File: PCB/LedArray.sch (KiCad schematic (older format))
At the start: 20 parts, among them Q2 2N3904, Q3 2N3904, Q4 2N3904, Q5 2N3904, Q6 2N3904

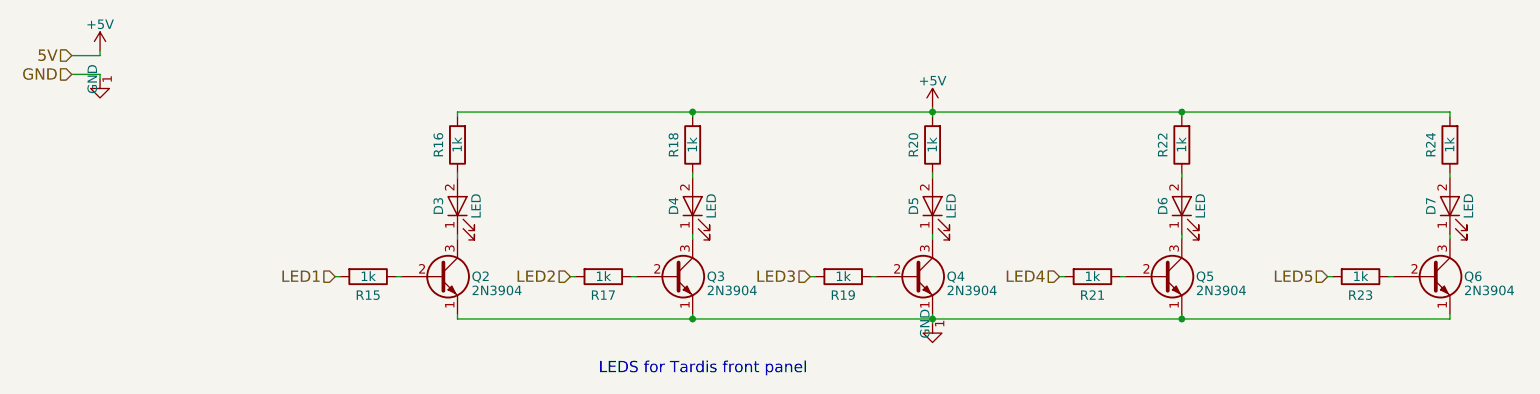
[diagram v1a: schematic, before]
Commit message: Added PCB layout
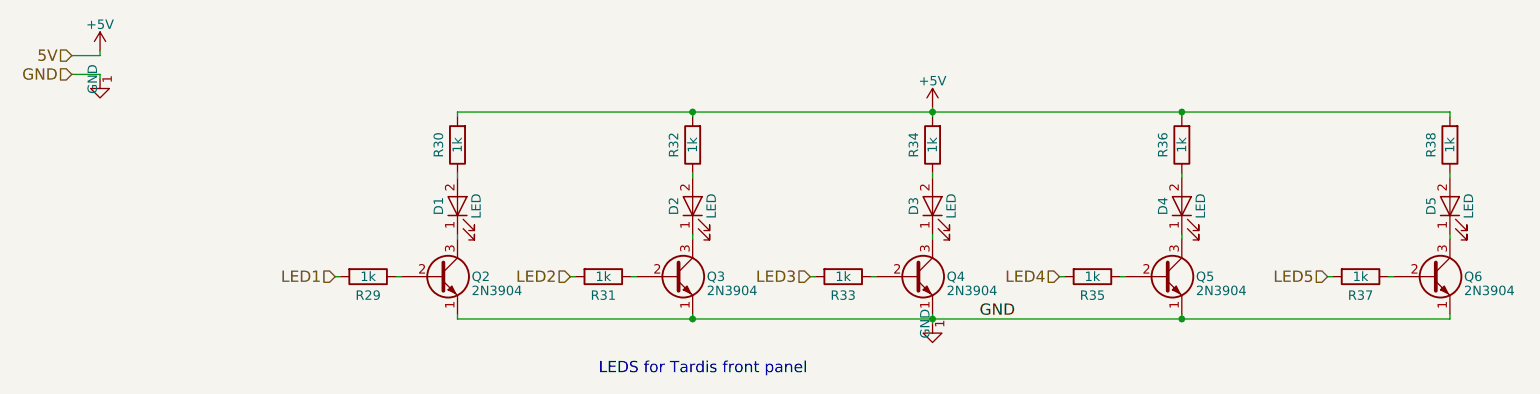
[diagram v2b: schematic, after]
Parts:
- D1: renamed from D3; footprint (none) -> LEDs:LED_D5.0mm
- D2: renamed from D4; footprint (none) -> LEDs:LED_D5.0mm
- D3: renamed from D5; footprint (none) -> LEDs:LED_D5.0mm
- D4: renamed from D6; footprint (none) -> LEDs:LED_D5.0mm
- D5: renamed from D7; footprint (none) -> LEDs:LED_D5.0mm
- Q2, Q3, Q4, Q5, Q6: footprint (none) -> TO_SOT_Packages_THT:TO-92_Molded_Narrow
- R29: renamed from R15; footprint (none) -> Resistors_SMD:R_0603_HandSoldering
- R30: renamed from R16; footprint (none) -> Resistors_SMD:R_0603_HandSoldering
- R31: renamed from R17; footprint (none) -> Resistors_SMD:R_0603_HandSoldering
- R32: renamed from R18; footprint (none) -> Resistors_SMD:R_0603_HandSoldering
- R33: renamed from R19; footprint (none) -> Resistors_SMD:R_0603_HandSoldering
- R34: renamed from R20; footprint (none) -> Resistors_SMD:R_0603_HandSoldering
- R35: renamed from R21; footprint (none) -> Resistors_SMD:R_0603_HandSoldering
- R36: renamed from R22; footprint (none) -> Resistors_SMD:R_0603_HandSoldering
- R37: renamed from R23; footprint (none) -> Resistors_SMD:R_0603_HandSoldering
- R38: renamed from R24; footprint (none) -> Resistors_SMD:R_0603_HandSoldering
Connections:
- net GND: now also Q2.1 (E), Q3.1 (E), Q4.1 (E), Q5.1 (E), Q6.1 (E)
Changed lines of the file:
@@
 $EndDescr
 $Comp
-L LED D7
+L LED D5
 U 1 1 5A1C9FD6
 P 8750 3800
-F 0 "D7" H 8750 3900 50  0000 C CNN
+F 0 "D5" H 8750 3900 50  0000 C CNN
 F 1 "LED" H 8750 3700 50  0000 C CNN
-F 2 "" H 8750 3800 50  0001 C CNN
+F 2 "LEDs:LED_D5.0mm" H 8750 3800 50  0001 C CNN
 F 3 "" H 8750 3800 50  0001 C CNN
 	1    8750 3800
@@
 $EndComp
 $Comp
-L R R24
+L R R38
 U 1 1 5A1C9FDD
 P 8750 3475
-F 0 "R24" V 8850 3475 50  0000 C CNN
+F 0 "R38" V 8850 3475 50  0000 C CNN
 F 1 "1k" V 8750 3475 50  0000 C CNN
-F 2 "" V 8680 3475 50  0001 C CNN
+F 2 "Resistors_SMD:R_0603_HandSoldering" V 8680 3475 50  0001 C CNN
 F 3 "" H 8750 3475 50  0001 C CNN
 	1    8750 3475
@@
 $EndComp
 $Comp
-L R R23
+L R R37
 U 1 1 5A1C9FE4
 P 8275 4175
-F 0 "R23" V 8375 4175 50  0000 C CNN
+F 0 "R37" V 8375 4175 50  0000 C CNN
 F 1 "1k" V 8275 4175 50  0000 C CNN
-F 2 "" V 8205 4175 50  0001 C CNN
+F 2 "Resistors_SMD:R_0603_HandSoldering" V 8205 4175 50  0001 C CNN
 F 3 "" H 8275 4175 50  0001 C CNN
 	1    8275 4175
@@
 	8750 3625 8750 3650
 $Comp
-L LED D6
+L LED D4
 U 1 1 5A1CA001
 P 7325 3800
-F 0 "D6" H 7325 3900 50  0000 C CNN
+F 0 "D4" H 7325 3900 50  0000 C CNN
 F 1 "LED" H 7325 3700 50  0000 C CNN
-F 2 "" H 7325 3800 50  0001 C CNN
+F 2 "LEDs:LED_D5.0mm" H 7325 3800 50  0001 C CNN
 F 3 "" H 7325 3800 50  0001 C CNN
 	1    7325 3800
@@
 $EndComp
 $Comp
-L R R22
+L R R36
 U 1 1 5A1CA008
 P 7325 3475
-F 0 "R22" V 7425 3475 50  0000 C CNN
+F 0 "R36" V 7425 3475 50  0000 C CNN
 F 1 "1k" V 7325 3475 50  0000 C CNN
-F 2 "" V 7255 3475 50  0001 C CNN
+F 2 "Resistors_SMD:R_0603_HandSoldering" V 7255 3475 50  0001 C CNN
 F 3 "" H 7325 3475 50  0001 C CNN
 	1    7325 3475
@@
 $EndComp
 $Comp
-L R R21
+L R R35
 U 1 1 5A1CA00F
 P 6850 4175
-F 0 "R21" V 6950 4175 50  0000 C CNN
+F 0 "R35" V 6950 4175 50  0000 C CNN
 F 1 "1k" V 6850 4175 50  0000 C CNN
-F 2 "" V 6780 4175 50  0001 C CNN
+F 2 "Resistors_SMD:R_0603_HandSoldering" V 6780 4175 50  0001 C CNN
 F 3 "" H 6850 4175 50  0001 C CNN
 	1    6850 4175
@@
 	7325 3625 7325 3650
 $Comp
-L LED D5
+L LED D3
 U 1 1 5A1CA02C
 P 6000 3800
-F 0 "D5" H 6000 3900 50  0000 C CNN
+F 0 "D3" H 6000 3900 50  0000 C CNN
 F 1 "LED" H 6000 3700 50  0000 C CNN
-F 2 "" H 6000 3800 50  0001 C CNN
+F 2 "LEDs:LED_D5.0mm" H 6000 3800 50  0001 C CNN
 F 3 "" H 6000 3800 50  0001 C CNN
 	1    6000 3800
@@
 $EndComp
 $Comp
-L R R20
+L R R34
 U 1 1 5A1CA033
 P 6000 3475
-F 0 "R20" V 6100 3475 50  0000 C CNN
+F 0 "R34" V 6100 3475 50  0000 C CNN
 F 1 "1k" V 6000 3475 50  0000 C CNN
-F 2 "" V 5930 3475 50  0001 C CNN
+F 2 "Resistors_SMD:R_0603_HandSoldering" V 5930 3475 50  0001 C CNN
 F 3 "" H 6000 3475 50  0001 C CNN
 	1    6000 3475
@@
 $EndComp
 $Comp
-L R R19
+L R R33
 U 1 1 5A1CA03A
 P 5525 4175
-F 0 "R19" V 5625 4175 50  0000 C CNN
+F 0 "R33" V 5625 4175 50  0000 C CNN
 F 1 "1k" V 5525 4175 50  0000 C CNN
-F 2 "" V 5455 4175 50  0001 C CNN
+F 2 "Resistors_SMD:R_0603_HandSoldering" V 5455 4175 50  0001 C CNN
 F 3 "" H 5525 4175 50  0001 C CNN
 	1    5525 4175
@@
 	6000 3625 6000 3650
 $Comp
-L LED D4
+L LED D2
 U 1 1 5A1CA057
 P 4725 3800
-F 0 "D4" H 4725 3900 50  0000 C CNN
+F 0 "D2" H 4725 3900 50  0000 C CNN
 F 1 "LED" H 4725 3700 50  0000 C CNN
-F 2 "" H 4725 3800 50  0001 C CNN
+F 2 "LEDs:LED_D5.0mm" H 4725 3800 50  0001 C CNN
 F 3 "" H 4725 3800 50  0001 C CNN
 	1    4725 3800
@@
 $EndComp
 $Comp
-L R R18
+L R R32
 U 1 1 5A1CA05E
 P 4725 3475
-F 0 "R18" V 4825 3475 50  0000 C CNN
+F 0 "R32" V 4825 3475 50  0000 C CNN
 F 1 "1k" V 4725 3475 50  0000 C CNN
-F 2 "" V 4655 3475 50  0001 C CNN
+F 2 "Resistors_SMD:R_0603_HandSoldering" V 4655 3475 50  0001 C CNN
 F 3 "" H 4725 3475 50  0001 C CNN
 	1    4725 3475
@@
 $EndComp
 $Comp
-L R R17
+L R R31
 U 1 1 5A1CA065
 P 4250 4175
-F 0 "R17" V 4350 4175 50  0000 C CNN
+F 0 "R31" V 4350 4175 50  0000 C CNN
 F 1 "1k" V 4250 4175 50  0000 C CNN
-F 2 "" V 4180 4175 50  0001 C CNN
+F 2 "Resistors_SMD:R_0603_HandSoldering" V 4180 4175 50  0001 C CNN
 F 3 "" H 4250 4175 50  0001 C CNN
 	1    4250 4175
@@
 	4725 3625 4725 3650
 $Comp
-L LED D3
+L LED D1
 U 1 1 5A1CA082
 P 3475 3800
-F 0 "D3" H 3475 3900 50  0000 C CNN
+F 0 "D1" H 3475 3900 50  0000 C CNN
 F 1 "LED" H 3475 3700 50  0000 C CNN
-F 2 "" H 3475 3800 50  0001 C CNN
+F 2 "LEDs:LED_D5.0mm" H 3475 3800 50  0001 C CNN
 F 3 "" H 3475 3800 50  0001 C CNN
 	1    3475 3800
@@
 $EndComp
 $Comp
-L R R16
+L R R30
 U 1 1 5A1CA089
 P 3475 3475
-F 0 "R16" V 3575 3475 50  0000 C CNN
+F 0 "R30" V 3575 3475 50  0000 C CNN
 F 1 "1k" V 3475 3475 50  0000 C CNN
-F 2 "" V 3405 3475 50  0001 C CNN
+F 2 "Resistors_SMD:R_0603_HandSoldering" V 3405 3475 50  0001 C CNN
 F 3 "" H 3475 3475 50  0001 C CNN
 	1    3475 3475
@@
 $EndComp
 $Comp
-L R R15
+L R R29
 U 1 1 5A1CA090
 P 3000 4175
-F 0 "R15" V 3100 4175 50  0000 C CNN
+F 0 "R29" V 3100 4175 50  0000 C CNN
 F 1 "1k" V 3000 4175 50  0000 C CNN
-F 2 "" V 2930 4175 50  0001 C CNN
+F 2 "Resistors_SMD:R_0603_HandSoldering" V 2930 4175 50  0001 C CNN
 F 3 "" H 3000 4175 50  0001 C CNN
 	1    3000 4175
@@
 GND
 $Comp
-L GND-RESCUE-Tardis #PWR059
+L GND-RESCUE-Tardis #PWR058
 U 1 1 5A34958F
 P 1575 3125
-AR Path="/5A34958F" Ref="#PWR059"  Part="1"
-AR Path="/5A1C89E5/5A34958F" Ref="#PWR63"  Part="1"
-F 0 "#PWR63" H 1575 2875 50  0001 C CNN
+F 0 "#PWR058" H 1575 2875 50  0001 C CNN
 F 1 "GND" H 1575 2975 50  0001 C CNN
 F 2 "" H 1575 3125 50  0001 C CNN
@@
 	1575 3100 1575 3125
 $Comp
-L +5V #PWR62
+L +5V #PWR059
 U 1 1 5A349597
 P 1575 2975
-F 0 "#PWR62" H 1575 2825 50  0001 C CNN
+F 0 "#PWR059" H 1575 2825 50  0001 C CNN
 F 1 "+5V" H 1575 3115 50  0000 C CNN
 F 2 "" H 1575 2975 50  0001 C CNN
@@
 	1575 3000 1575 2975
 $Comp
-L +5V #PWR64
+L +5V #PWR060
 U 1 1 5A349B68
 P 6000 3275
-F 0 "#PWR64" H 6000 3125 50  0001 C CNN
+F 0 "#PWR060" H 6000 3125 50  0001 C CNN
 F 1 "+5V" H 6000 3415 50  0000 C CNN
 F 2 "" H 6000 3275 50  0001 C CNN
@@
 $EndComp
 $Comp
-L GND-RESCUE-Tardis #PWR062
+L GND-RESCUE-Tardis #PWR061
 U 1 1 5A349BAF
 P 6000 4425
-AR Path="/5A349BAF" Ref="#PWR062"  Part="1"
-AR Path="/5A1C89E5/5A349BAF" Ref="#PWR65"  Part="1"
-F 0 "#PWR65" H 6000 4175 50  0001 C CNN
+F 0 "#PWR061" H 6000 4175 50  0001 C CNN
 F 1 "GND" H 6000 4275 50  0001 C CNN
 F 2 "" H 6000 4425 50  0001 C CNN
@@
 F 0 "Q2" H 3550 4175 50  0000 L CNN
 F 1 "2N3904" H 3550 4100 50  0000 L CNN
-F 2 "" H 3575 4275 50  0001 C CNN
+F 2 "TO_SOT_Packages_THT:TO-92_Molded_Narrow" H 3575 4275 50  0001 C CNN
 F 3 "" H 3375 4175 50  0001 C CNN
 	1    3375 4175
@@
 F 0 "Q3" H 4800 4175 50  0000 L CNN
 F 1 "2N3904" H 4800 4100 50  0000 L CNN
-F 2 "" H 4825 4275 50  0001 C CNN
+F 2 "TO_SOT_Packages_THT:TO-92_Molded_Narrow" H 4825 4275 50  0001 C CNN
 F 3 "" H 4625 4175 50  0001 C CNN
 	1    4625 4175
@@
 F 0 "Q4" H 6075 4175 50  0000 L CNN
 F 1 "2N3904" H 6075 4100 50  0000 L CNN
-F 2 "" H 6100 4275 50  0001 C CNN
+F 2 "TO_SOT_Packages_THT:TO-92_Molded_Narrow" H 6100 4275 50  0001 C CNN
 F 3 "" H 5900 4175 50  0001 C CNN
 	1    5900 4175
@@
 F 0 "Q5" H 7400 4175 50  0000 L CNN
 F 1 "2N3904" H 7400 4100 50  0000 L CNN
-F 2 "" H 7425 4275 50  0001 C CNN
+F 2 "TO_SOT_Packages_THT:TO-92_Molded_Narrow" H 7425 4275 50  0001 C CNN
 F 3 "" H 7225 4175 50  0001 C CNN
 	1    7225 4175
@@
 F 0 "Q6" H 8825 4175 50  0000 L CNN
 F 1 "2N3904" H 8825 4100 50  0000 L CNN
-F 2 "" H 8850 4275 50  0001 C CNN
+F 2 "TO_SOT_Packages_THT:TO-92_Molded_Narrow" H 8850 4275 50  0001 C CNN
 F 3 "" H 8650 4175 50  0001 C CNN
 	1    8650 4175
 	1    0    0    -1
 $EndComp
+Text Label 6250 4400 0    60   ~ 0
+GND
 $EndSCHEMATC
